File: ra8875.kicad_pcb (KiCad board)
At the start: 2 copper layers, 6 parts

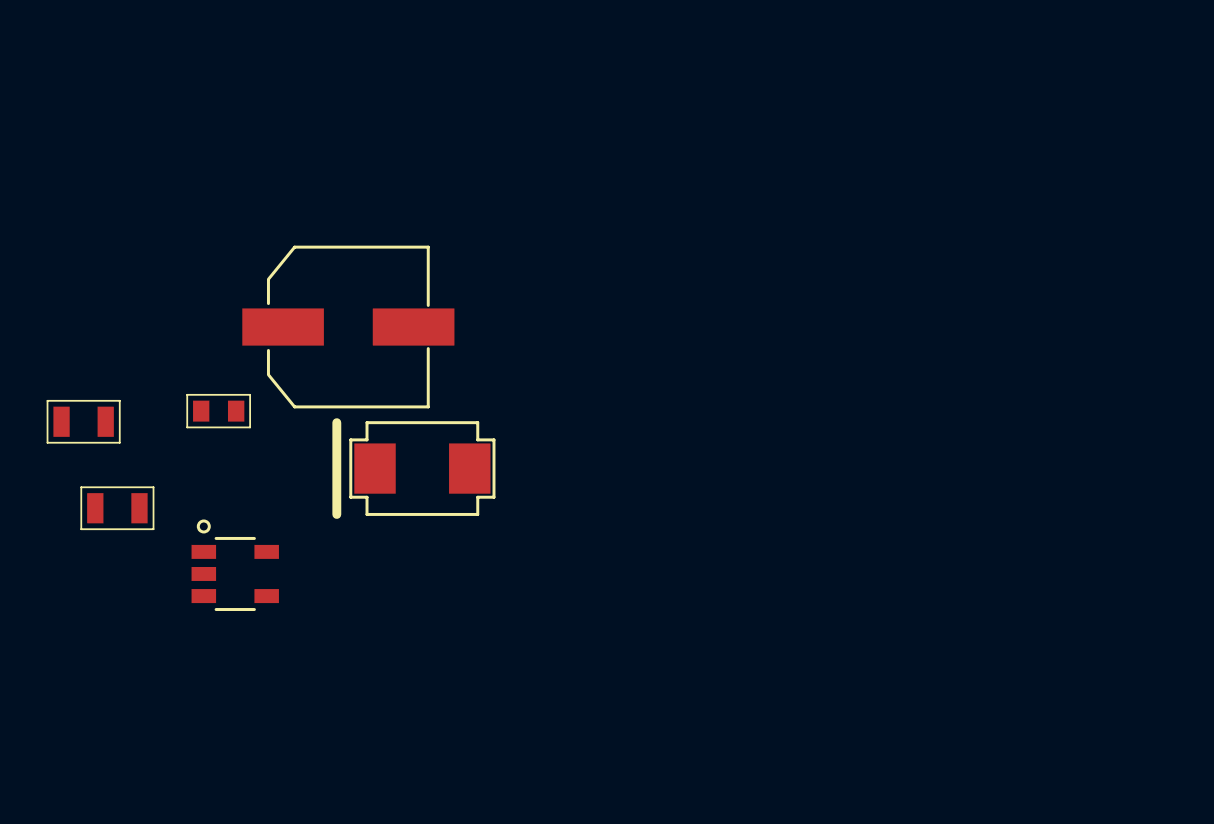
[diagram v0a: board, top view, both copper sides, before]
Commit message: Add datasheets, appnotes and also completes the preliminary design for the TPS61040 power supply for the LCD backlight
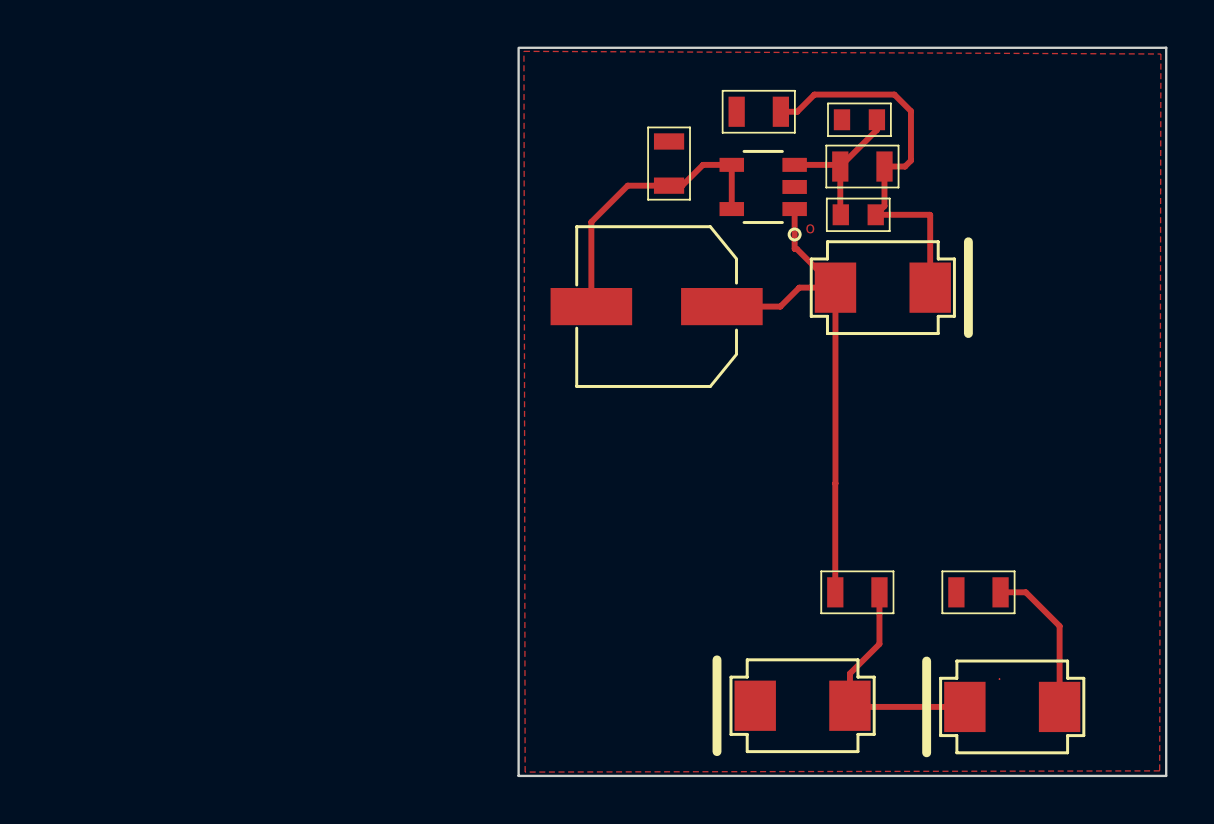
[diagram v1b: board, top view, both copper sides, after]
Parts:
- added C3: 1uF, 0805, F.Cu at (78.0, 23.1)
- added C4: 1uF, 0805, F.Cu at (82.2, 43.7)
- added C5: 4.7uF, 0805, F.Cu at (87.4, 43.7)
- added D2: ZENER, DO-214AA, F.Cu at (79.9, 48.6)
- added D3: ZENER, DO-214AA, F.Cu at (88.9, 48.7)
- added R2: 210K, 0603, F.Cu at (82.3, 23.5)
- C1: value C -> 4.7uF
- C2: value C -> 22pF
- R1: value R -> 1.5M
- moved C2 35.1 mm to (82.4, 25.5), turned to 180 degrees
- moved R1 28.7 mm to (82.3, 27.5), turned to 180 degrees
- moved TPS1 28.1 mm to (78.2, 26.4), turned to 90 degrees
- moved C1 27.9 mm to (74.2, 25.3), turned to 90 degrees
- moved D1 21.2 mm to (83.3, 30.7), turned to 180 degrees
- moved L1 13.2 mm to (73.6, 31.5), turned to 180 degrees
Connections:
- C2 pad 1: GND -> Net-(C2-Pad1)
- D1 pad 2: GND -> Net-(C2-Pad1)
- R1 pad 1: GND -> Net-(C2-Pad1)
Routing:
- net Net-(C4-Pad2): track 0.00 -> 22.4 mm
- net Net-(C2-Pad1): track 0.00 -> 17.2 mm
- net Net-(C1-Pad1): track 0.00 -> 12.6 mm
- net Net-(C4-Pad1): track 0.00 -> 10.3 mm
- net Net-(C2-Pad2): track 0.00 -> 6.72 mm
- net Net-(C5-Pad1): track 0.00 -> 6.60 mm
- added copper zone on F.Cu, net GND
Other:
- board outline added: 27.8 x 31.2 mm
- rule trace_min: 0.254 -> 0
- board text added: "o"

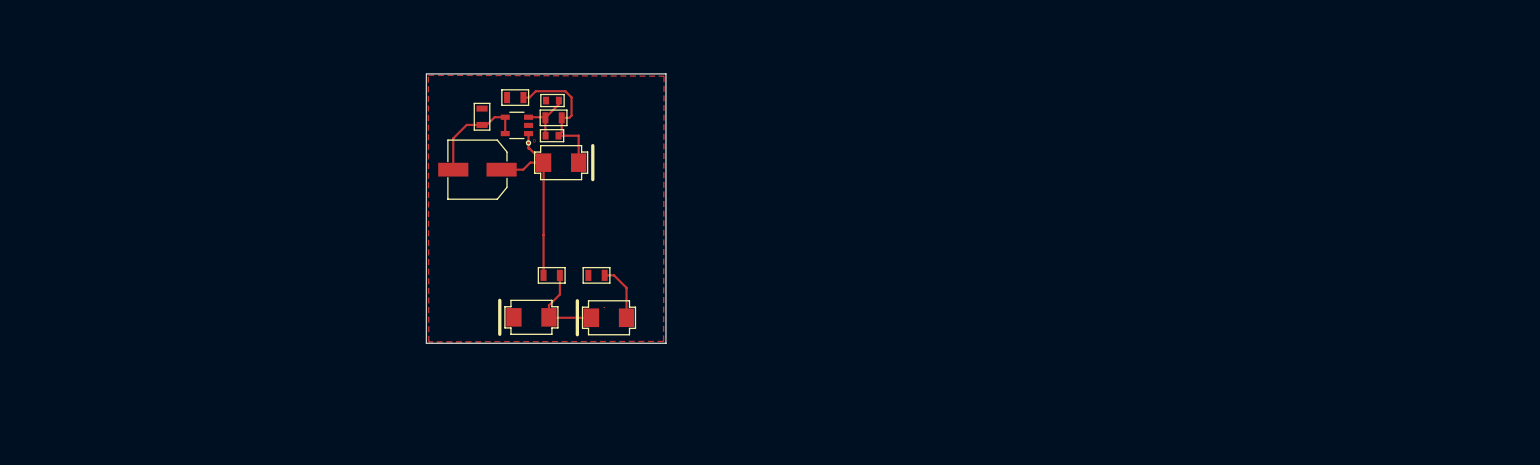
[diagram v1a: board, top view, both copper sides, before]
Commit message: TPS61040 test board completed, update the kicad footprint .pdf from qi-hardware website
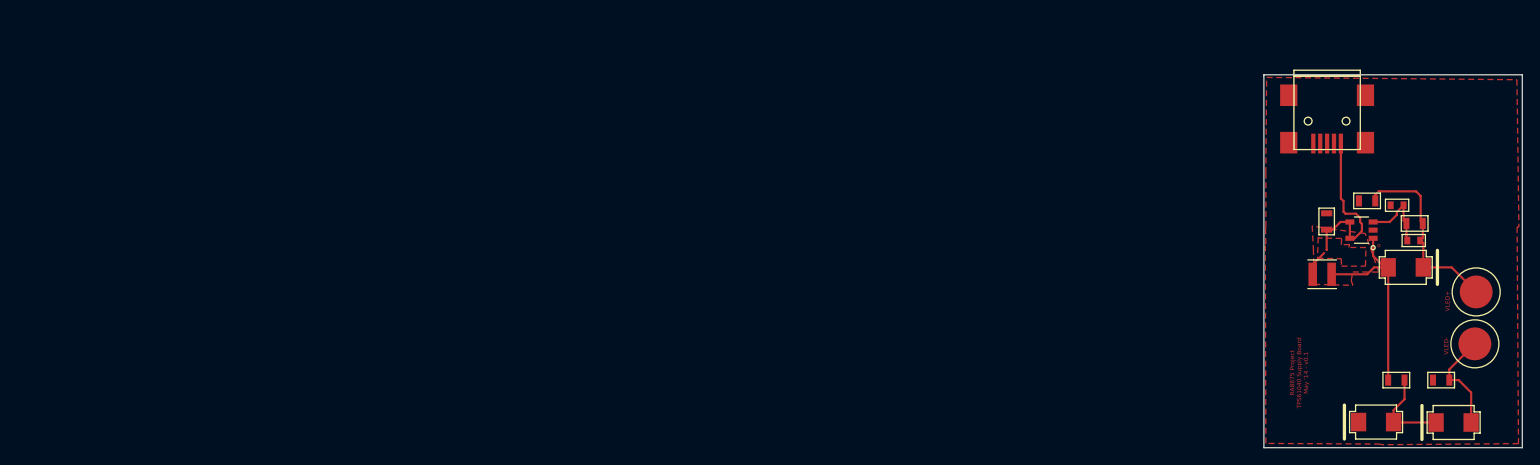
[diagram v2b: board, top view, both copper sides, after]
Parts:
- added PAD_C_150x150: Val*, PAD_C_150x150, F.Cu at (189.4, 45.7)
- added PAD_C_150x150: Val*, PAD_C_150x150, F.Cu at (189.3, 51.7)
- added miniUSB_B: Val*, miniUSB_B, F.Cu at (172.1, 29.6)
- L1: footprint c-smd-6.3mmx8mm -> INDUCTOR-2P-3mmx3mm
- moved R1 100.6 mm to (182.2, 39.7)
- moved C2 100.6 mm to (182.3, 37.7)
- moved C3 99.5 mm to (176.8, 35.1)
- moved L1 98.7 mm to (171.6, 43.6), turned to 90 degrees
- moved C1 98.7 mm to (172.1, 37.5)
- moved D2 98.7 mm to (177.8, 60.7)
- moved R2 98.7 mm to (180.2, 35.6)
- moved D1 98.7 mm to (181.2, 42.8)
- moved C4 98.7 mm to (180.1, 55.9)
- moved C5 98.7 mm to (185.3, 55.9)
- moved D3 98.7 mm to (186.8, 60.8)
- moved TPS1 98.7 mm to (176.1, 38.5)
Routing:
- net Net-(C1-Pad1): track 12.6 -> 23.9 mm
- net Net-(C5-Pad1): track 6.60 -> 12.0 mm
- net Net-(C2-Pad1): track 17.2 -> 22.3 mm
- net Net-(C2-Pad2): track 6.72 -> 8.79 mm
- net Net-(C4-Pad2): track 22.4 -> 24.3 mm
- added copper zone on F.Cu, net Net-(C1-Pad1)
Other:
- board size 27.8 x 31.2 mm -> 30 x 43.2 mm
- board text added: "RA8875 Project TPS61040 Supply Board May '14 - v0.1"
- board text added: "VLED+"
- board text added: "VLED-"

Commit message: Modification to input track 0.5mm, add USB port and power point (+,-) and change layout
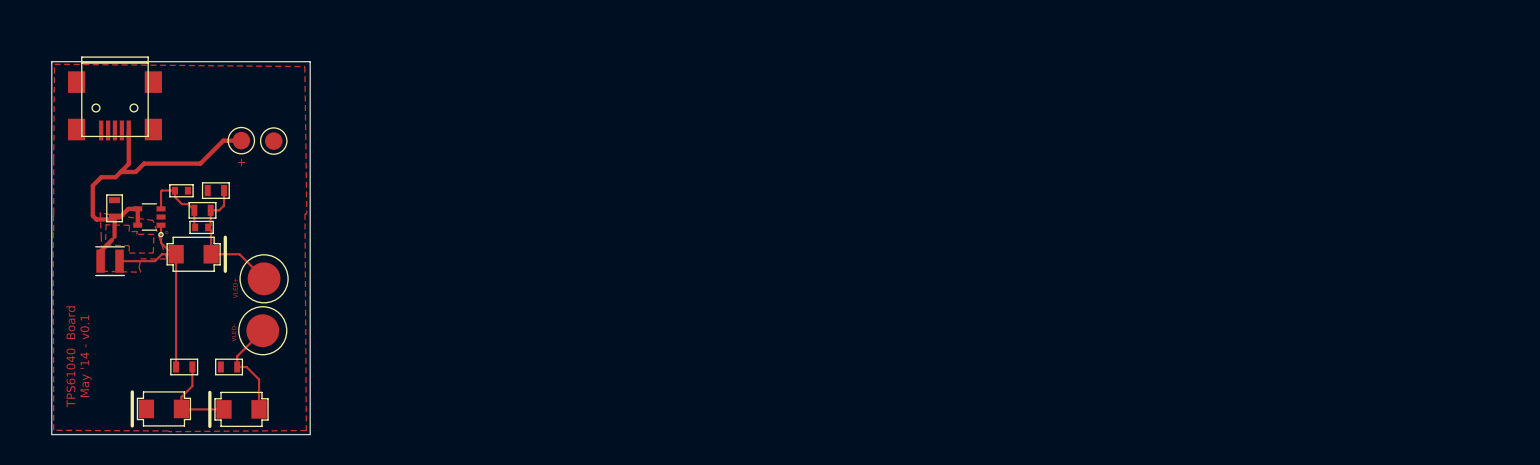
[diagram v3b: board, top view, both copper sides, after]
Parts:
- added ?: Val*, PAD_C_80x80, F.Cu at (46.2, 28.1)
- added ?: Val*, PAD_C_80x80, F.Cu at (50.0, 28.2)
- moved R2 140.9 mm to (39.3, 33.9), turned to 0 degrees
- moved C1 140.5 mm to (31.6, 36.0)
- moved D1 140.5 mm to (40.7, 41.3)
- moved D2 140.5 mm to (37.3, 59.2)
- moved L1 140.5 mm to (31.0, 42.1)
- moved PAD_C_150x150 140.5 mm to (48.9, 44.1)
- moved PAD_C_150x150 140.5 mm to (48.7, 50.2)
- moved R1 140.5 mm to (41.6, 38.2)
- moved ? 140.5 mm to (31.6, 28.1)
- moved C2 140.5 mm to (41.8, 36.2)
- moved C4 140.5 mm to (39.6, 54.4)
- moved C5 140.5 mm to (44.8, 54.4)
- moved D3 140.5 mm to (46.3, 59.3)
- moved TPS1 140.5 mm to (35.6, 37.0)
- moved C3 133.5 mm to (43.3, 33.9)
- renumbered miniUSB_B to ?
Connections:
- ? pad 1: (no net) -> Net-(C1-Pad1)
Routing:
- net Net-(C1-Pad1): track 23.9 -> 41.2 mm
- net Net-(C2-Pad1): track 22.3 -> 16.2 mm
- net Net-(C2-Pad2): track 8.79 -> 9.33 mm
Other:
- net class PoweSupply added: clearance 0.254, trace_width 0.5, via_dia 0.889, via_drill 0.635
- board text added: "+"
- board text added: "TPS61040 Board May '14 - v0.1"
- board text removed: "RA8875 Project TPS61040 Supply Board May '14 - v0.1"

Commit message: Modify the layout and traces connecting pin 1 and 5
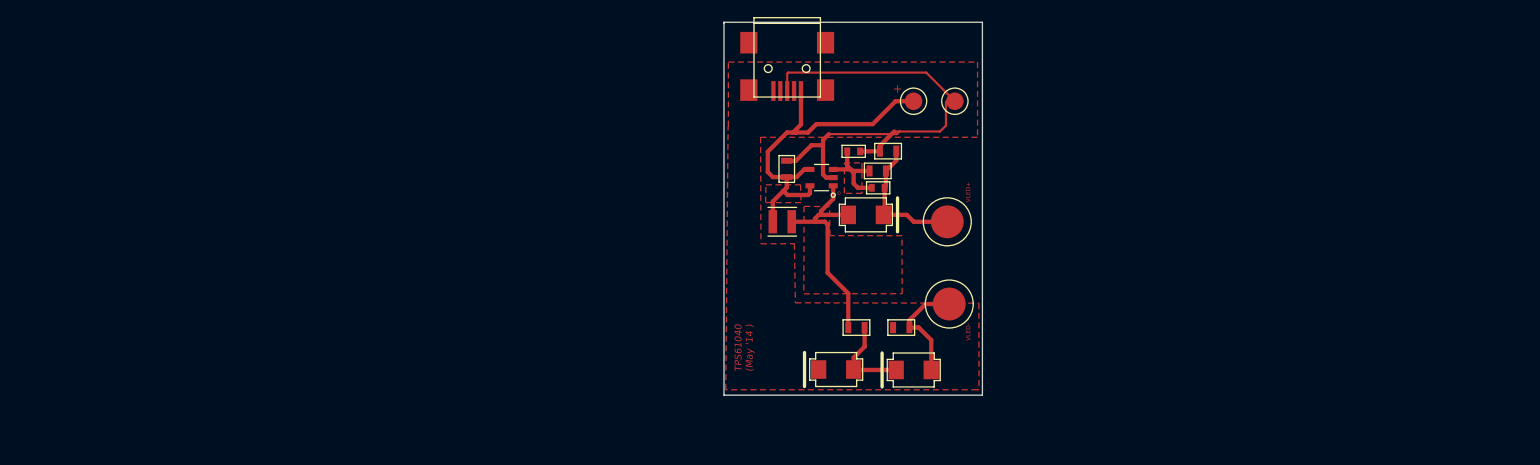
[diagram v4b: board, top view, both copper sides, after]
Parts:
- moved PAD_C_150x150 79.6 mm to (128.3, 47.1)
- moved PAD_C_150x150 79.5 mm to (128.1, 37.5)
- moved ? 79.1 mm to (129.0, 23.6)
- moved R1 78.6 mm to (120.1, 33.6)
- moved C2 78.4 mm to (120.0, 31.6)
- moved ? 78.1 mm to (109.5, 23.5)
- moved ? 78.1 mm to (124.2, 23.6)
- moved C3 78.1 mm to (121.2, 29.3)
- moved C4 78.1 mm to (117.6, 49.8)
- moved C5 78.1 mm to (122.8, 49.8)
- moved D1 78.1 mm to (118.7, 36.7)
- moved D3 78.1 mm to (124.2, 54.7)
- moved L1 78.1 mm to (109.0, 37.5)
- moved TPS1 78.1 mm to (113.5, 32.4)
- moved C1 78.1 mm to (109.5, 31.4)
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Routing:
- net GND: track 0.00 -> 56.8 mm
- net Net-(C2-Pad2): track 9.33 -> 11.1 mm
- net Net-(C1-Pad1): track 41.2 -> 42.9 mm
- net Net-(C4-Pad2): track 24.3 -> 25.6 mm
- net Net-(C5-Pad1): track 12.0 -> 12.8 mm
- added copper zone on F.Cu, net Net-(C2-Pad2)
- added copper zone on F.Cu, net Net-(C4-Pad2)
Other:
- board text added: "TPS61040 (May '14 )"
- board text removed: "TPS61040 Board May '14 - v0.1"

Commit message: Made changes to size of inductor, capacitors, tracks and few other details
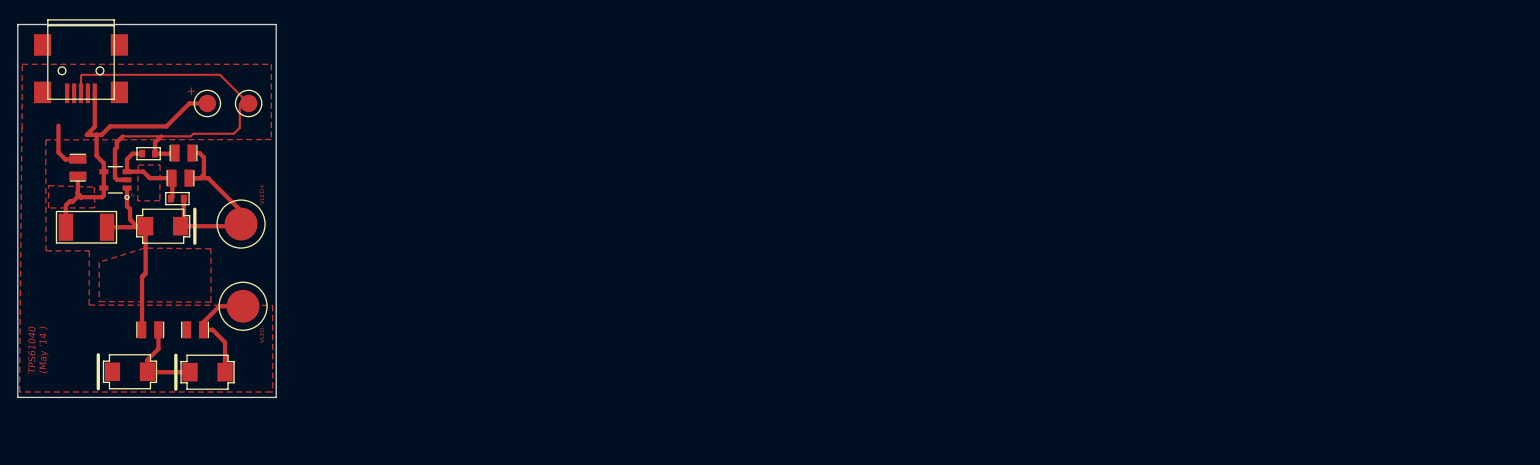
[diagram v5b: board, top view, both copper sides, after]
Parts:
- C1, C2, C3, C4, C5: footprint 0805 -> 0805SMDLED_BIGGER
- L1: footprint INDUCTOR-2P-3mmx3mm -> 1812
- moved C1 82.2 mm to (27.3, 31.2)
- moved ? 81.9 mm to (27.7, 23.8)
- moved ? 81.9 mm to (42.3, 23.8)
- moved ? 81.9 mm to (47.1, 23.8)
- moved C4 81.9 mm to (35.7, 50.0)
- moved C5 81.9 mm to (40.9, 50.0)
- moved D3 81.9 mm to (42.3, 55.0)
- moved PAD_C_150x150 81.9 mm to (46.2, 37.8)
- moved TPS1 81.9 mm to (31.7, 32.7)
- moved D2 81.9 mm to (33.3, 54.9)
- moved PAD_C_150x150 81.9 mm to (46.5, 47.3)
- moved R2 81.7 mm to (35.5, 29.6)
- moved C3 81.7 mm to (39.5, 29.6)
- moved D1 81.5 mm to (37.2, 38.0)
- moved R1 81.2 mm to (38.8, 34.8)
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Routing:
- net Net-(C2-Pad1): track 15.7 -> 25.2 mm
- net Net-(C1-Pad1): track 42.9 -> 38.4 mm
- net Net-(C4-Pad2): track 25.6 -> 23.2 mm
